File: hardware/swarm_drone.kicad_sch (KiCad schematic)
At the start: 8 parts

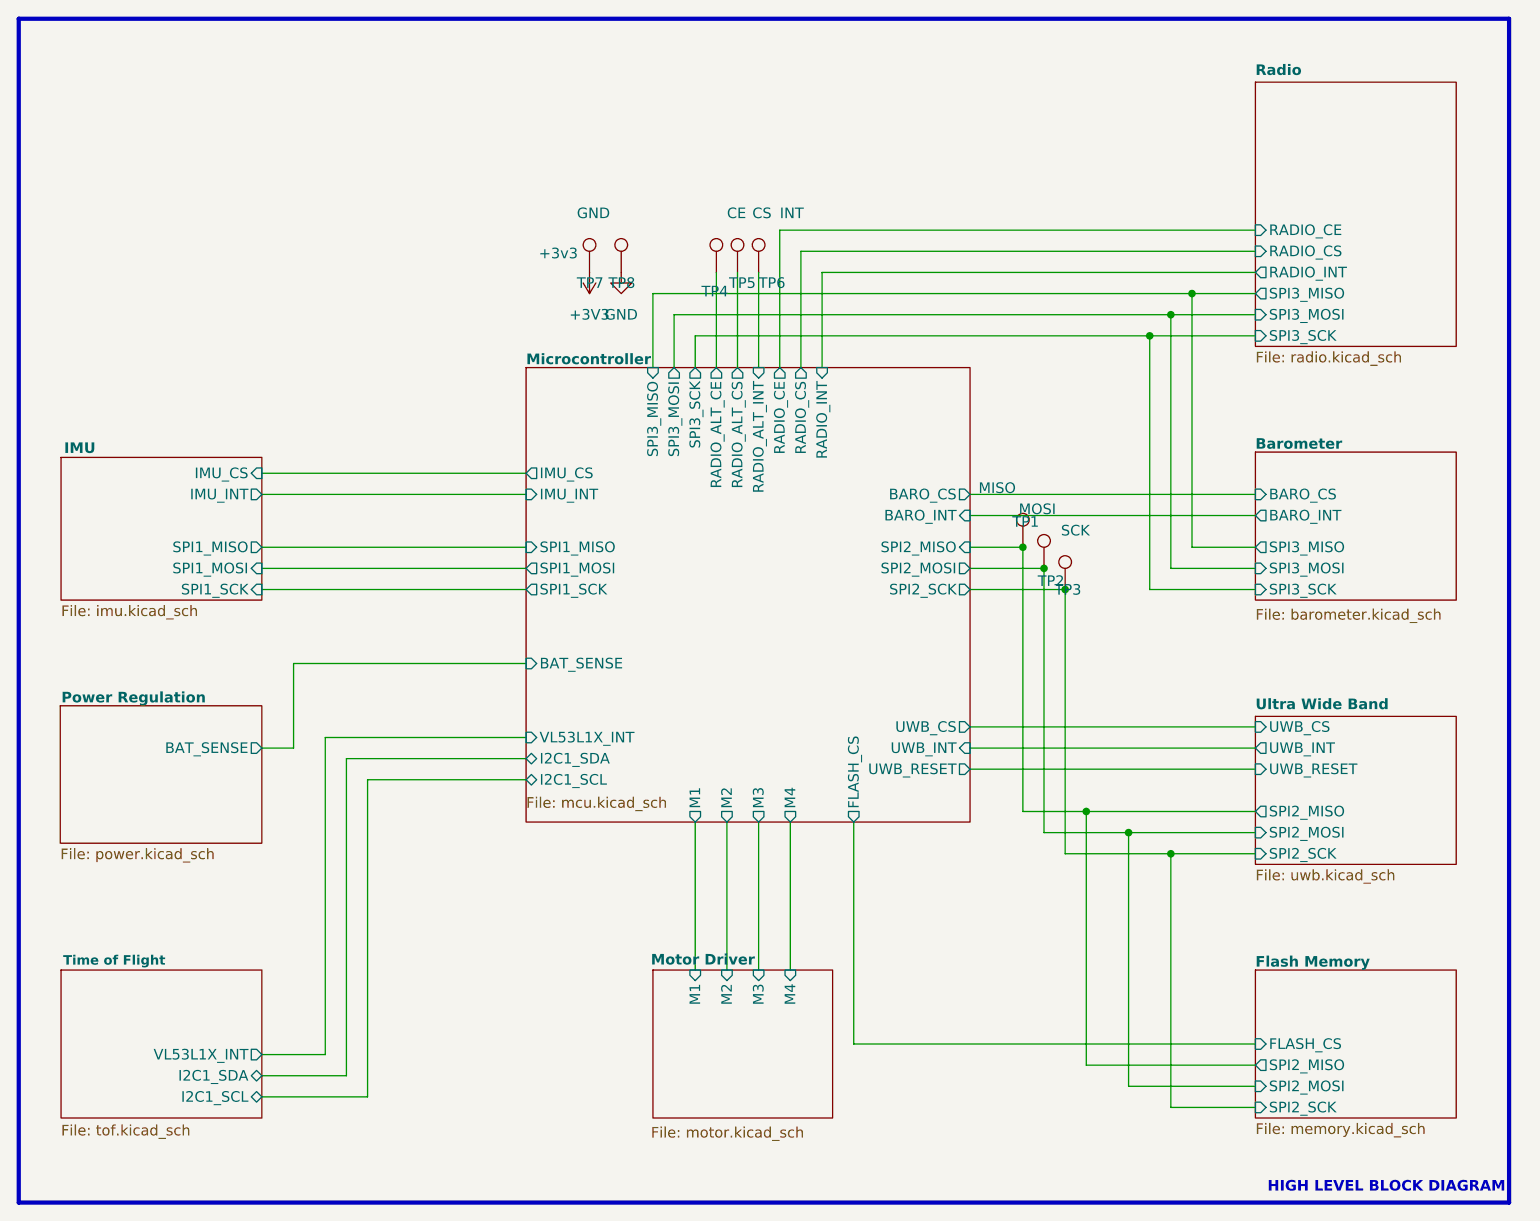
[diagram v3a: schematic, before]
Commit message: feat(kicad): Routing complete, assigning jlc components to each footprint
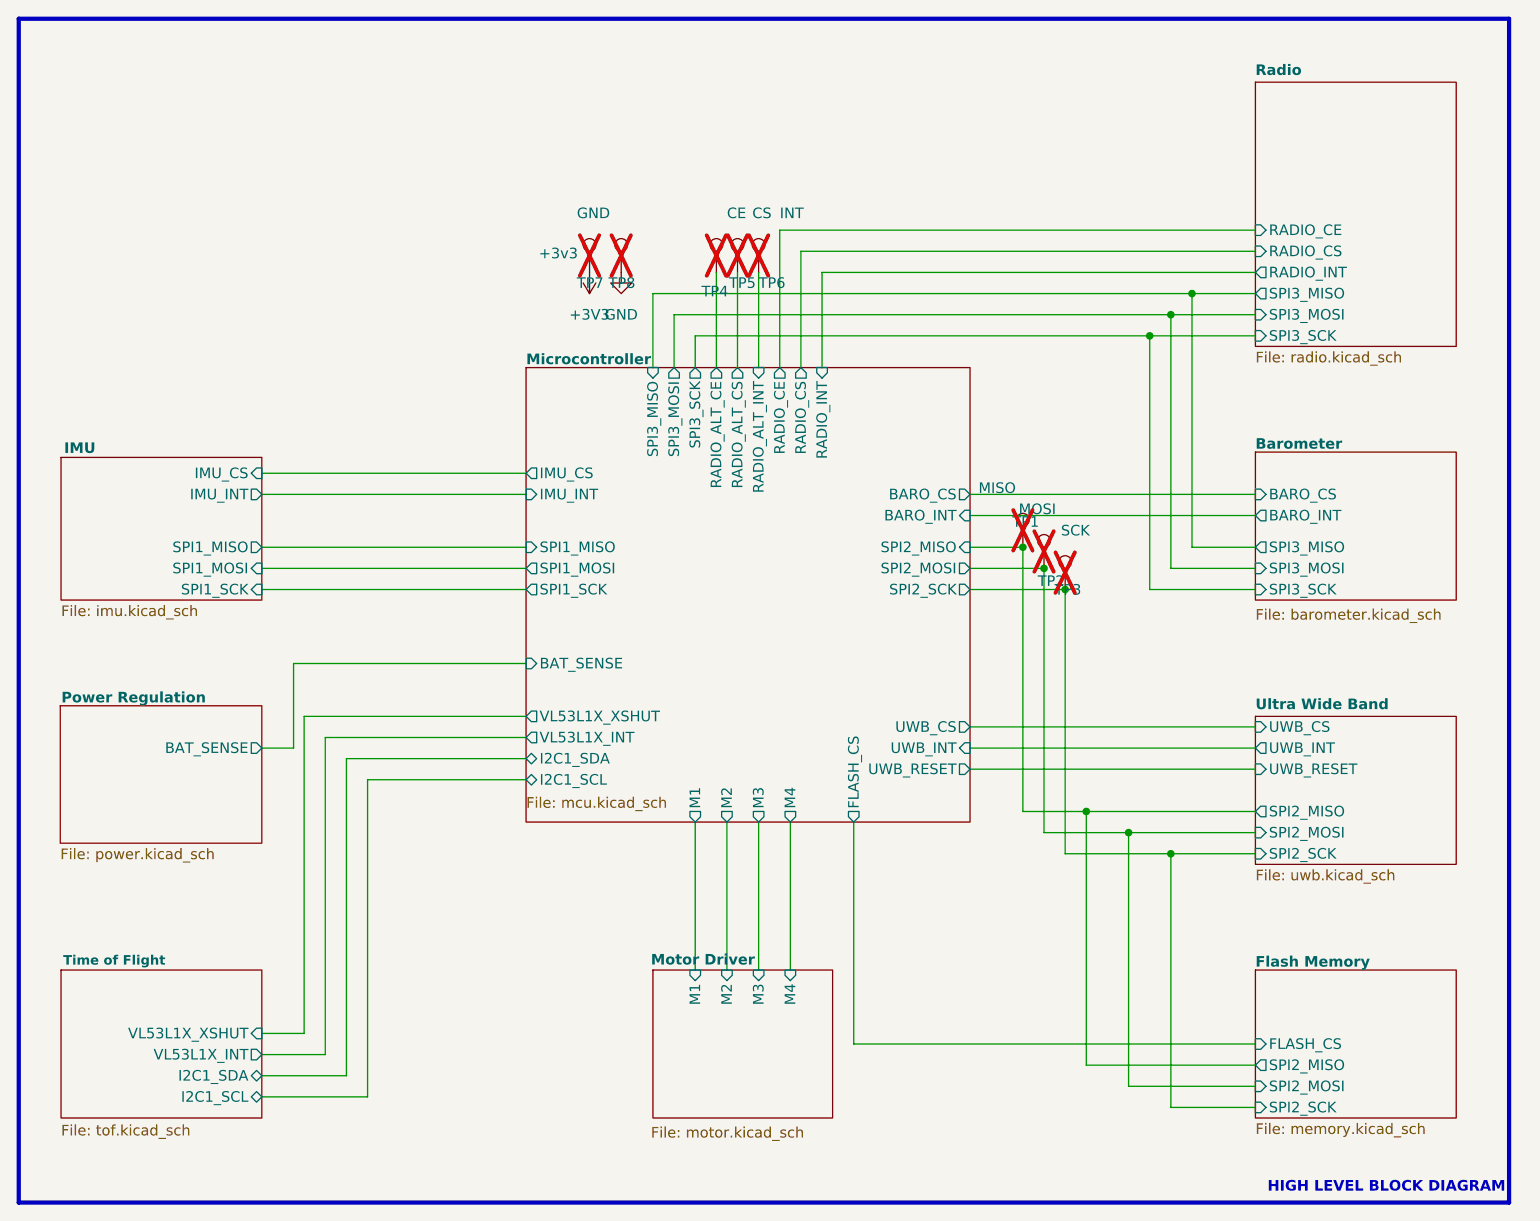
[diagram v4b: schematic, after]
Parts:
- TP1, TP2, TP3, TP4, TP5, TP6, TP7, TP8: now not fitted
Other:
- sheet Microcontroller ports: added VL53L1X_XSHUT; removed none
- sheet Time of Flight ports: added VL53L1X_XSHUT; removed none
